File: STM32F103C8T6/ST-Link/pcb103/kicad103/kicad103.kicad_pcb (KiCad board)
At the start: 4 copper layers, 20 parts, among them IC1 LD1117DT33TR, J1 0480372200, J2 Conn_01x02_Socket, U1 STM32F103C8T6, Y1 8MHz 20pF

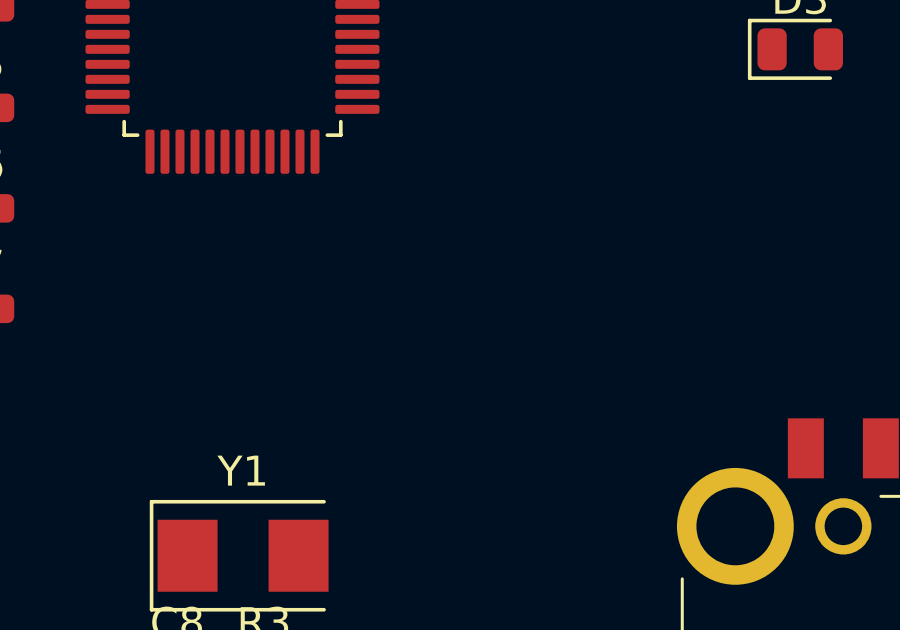
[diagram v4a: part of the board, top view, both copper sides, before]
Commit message: Pull-up resistor on USB_DP line
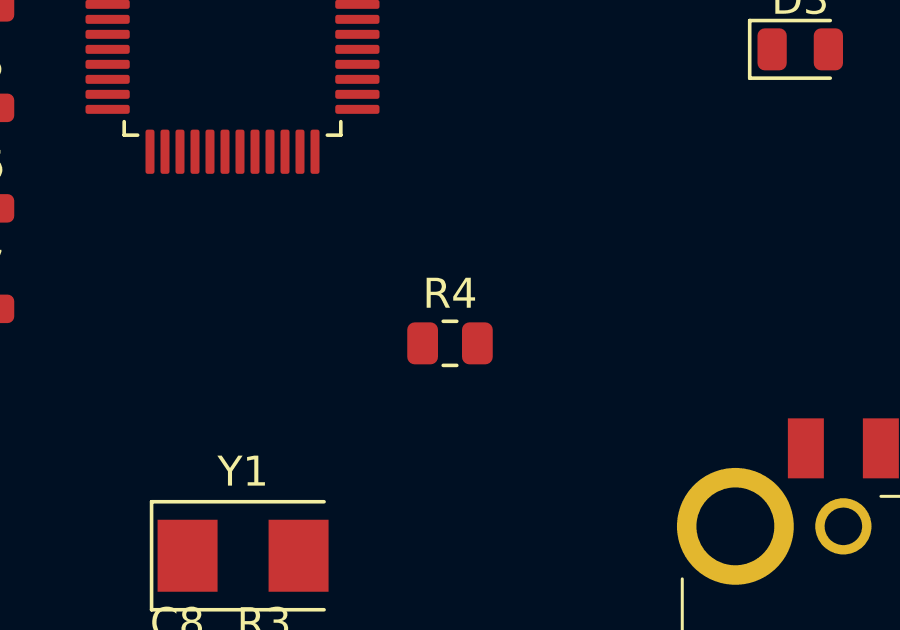
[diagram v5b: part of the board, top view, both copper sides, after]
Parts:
- added R4: 1k5, Resistor_SMD:R_0805_2012Metric, F.Cu at (196.6, 63.7)
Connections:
- net Net-(U1-VBAT) renamed +3.3V
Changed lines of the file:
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@@
   (net 0 "")
   (net 1 "Net-(D1-K)")
-  (net 2 "Net-(U1-VBAT)")
+  (net 2 "+3.3V")
   (net 3 "/USB_D-")
   (net 4 "GND")
@@
       (stroke (width 0.1) (type solid)) (layer "F.Fab"))
     (pad "1" smd roundrect (at -0.775 0) (size 0.9 0.95) (layers "F.Cu" "F.Paste" "F.Mask") (roundrect_rratio 0.25)
-      (net 2 "Net-(U1-VBAT)") (pintype "passive"))
+      (net 2 "+3.3V") (pintype "passive"))
     (pad "2" smd roundrect (at 0.775 0) (size 0.9 0.95) (layers "F.Cu" "F.Paste" "F.Mask") (roundrect_rratio 0.25)
       (net 4 "GND") (pintype "passive"))
@@
       (stroke (width 0.1) (type solid)) (layer "F.Fab"))
     (pad "1" smd roundrect (at -0.775 0) (size 0.9 0.95) (layers "F.Cu" "F.Paste" "F.Mask") (roundrect_rratio 0.25)
-      (net 2 "Net-(U1-VBAT)") (pintype "passive"))
+      (net 2 "+3.3V") (pintype "passive"))
     (pad "2" smd roundrect (at 0.775 0) (size 0.9 0.95) (layers "F.Cu" "F.Paste" "F.Mask") (roundrect_rratio 0.25)
       (net 4 "GND") (pintype "passive"))
@@
       (stroke (width 0.1) (type solid)) (layer "F.Fab"))
     (pad "1" smd roundrect (at -0.775 0) (size 0.9 0.95) (layers "F.Cu" "F.Paste" "F.Mask") (roundrect_rratio 0.25)
-      (net 2 "Net-(U1-VBAT)") (pintype "passive"))
+      (net 2 "+3.3V") (pintype "passive"))
     (pad "2" smd roundrect (at 0.775 0) (size 0.9 0.95) (layers "F.Cu" "F.Paste" "F.Mask") (roundrect_rratio 0.25)
       (net 4 "GND") (pintype "passive"))
@@
       (stroke (width 0.1) (type solid)) (layer "F.Fab"))
     (pad "1" smd roundrect (at -0.775 0) (size 0.9 0.95) (layers "F.Cu" "F.Paste" "F.Mask") (roundrect_rratio 0.25)
-      (net 2 "Net-(U1-VBAT)") (pintype "passive"))
+      (net 2 "+3.3V") (pintype "passive"))
     (pad "2" smd roundrect (at 0.775 0) (size 0.9 0.95) (layers "F.Cu" "F.Paste" "F.Mask") (roundrect_rratio 0.25)
       (net 4 "GND") (pintype "passive"))
@@
       (stroke (width 0.1) (type solid)) (layer "F.Fab"))
     (pad "1" smd roundrect (at -4.1625 -2.75) (size 1.475 0.3) (layers "F.Cu" "F.Paste" "F.Mask") (roundrect_rratio 0.25)
-      (net 2 "Net-(U1-VBAT)") (pinfunction "VBAT") (pintype "power_in"))
+      (net 2 "+3.3V") (pinfunction "VBAT") (pintype "power_in"))
     (pad "2" smd roundrect (at -4.1625 -2.25) (size 1.475 0.3) (layers "F.Cu" "F.Paste" "F.Mask") (roundrect_rratio 0.25)
       (net 50 "Net-(D3-A)") (pinfunction "PC13") (pintype "bidirectional"))
@@
       (net 4 "GND") (pinfunction "VSSA") (pintype "power_in"))
     (pad "9" smd roundrect (at -4.1625 1.25) (size 1.475 0.3) (layers "F.Cu" "F.Paste" "F.Mask") (roundrect_rratio 0.25)
-      (net 2 "Net-(U1-VBAT)") (pinfunction "VDDA") (pintype "power_in"))
+      (net 2 "+3.3V") (pinfunction "VDDA") (pintype "power_in"))
     (pad "10" smd roundrect (at -4.1625 1.75) (size 1.475 0.3) (layers "F.Cu" "F.Paste" "F.Mask") (roundrect_rratio 0.25)
       (net 18 "unconnected-(U1-PA0-Pad10)") (pinfunction "PA0") (pintype "bidirectional+no_connect"))
@@
       (net 4 "GND") (pinfunction "VSS") (pintype "power_in"))
     (pad "24" smd roundrect (at 2.75 4.1625) (size 0.3 1.475) (layers "F.Cu" "F.Paste" "F.Mask") (roundrect_rratio 0.25)
-      (net 2 "Net-(U1-VBAT)") (pinfunction "VDD") (pintype "power_in"))
+      (net 2 "+3.3V") (pinfunction "VDD") (pintype "power_in"))
     (pad "25" smd roundrect (at 4.1625 2.75) (size 1.475 0.3) (layers "F.Cu" "F.Paste" "F.Mask") (roundrect_rratio 0.25)
       (net 31 "unconnected-(U1-PB12-Pad25)") (pinfunction "PB12") (pintype "bidirectional+no_connect"))
@@
       (net 4 "GND") (pinfunction "VSS") (pintype "passive"))
     (pad "36" smd roundrect (at 4.1625 -2.75) (size 1.475 0.3) (layers "F.Cu" "F.Paste" "F.Mask") (roundrect_rratio 0.25)
-      (net 2 "Net-(U1-VBAT)") (pinfunction "VDD") (pintype "power_in"))
+      (net 2 "+3.3V") (pinfunction "VDD") (pintype "power_in"))
     (pad "37" smd roundrect (at 2.75 -4.1625) (size 0.3 1.475) (layers "F.Cu" "F.Paste" "F.Mask") (roundrect_rratio 0.25)
       (net 39 "unconnected-(U1-PA14-Pad37)") (pinfunction "PA14") (pintype "bidirectional+no_connect"))
@@
       (net 4 "GND") (pinfunction "VSS") (pintype "passive"))
     (pad "48" smd roundrect (at -2.75 -4.1625) (size 0.3 1.475) (layers "F.Cu" "F.Paste" "F.Mask") (roundrect_rratio 0.25)
-      (net 2 "Net-(U1-VBAT)") (pinfunction "VDD") (pintype "power_in"))
+      (net 2 "+3.3V") (pinfunction "VDD") (pintype "power_in"))
     (model "${KICAD6_3DMODEL_DIR}/Package_QFP.3dshapes/LQFP-48_7x7mm_P0.5mm.wrl"
       (offset (xyz 0 0 0))
@@
     )
   )
+  (footprint "Resistor_SMD:R_0805_2012Metric" (layer "F.Cu")
+    (at 196.5875 63.7)
+    (descr "Resistor SMD 0805 (2012 Metric), square (rectangular) end terminal, IPC_7351 nominal, (Body size source: IPC-SM-782 page 72, https://www.pcb-3d.com/wordpress/wp-content/uploads/ipc-sm-782a_amendment_1_and_2.pdf), generated with kicad-footprint-generator")
+    (tags "resistor")
+    (property "Sheetfile" "kicad103.kicad_sch")
+    (property "Sheetname" "")
+    (property "ki_description" "Resistor")
+    (property "ki_keywords" "R res resistor")
+    (attr smd)
+    (fp_text reference "R4" (at 0 -1.65) (layer "F.SilkS")
+        (effects (font (size 1 1) (thickness 0.15)))
+    )
+    (fp_text value "1k5" (at 0 1.65) (layer "F.Fab")
+        (effects (font (size 1 1) (thickness 0.15)))
+    )
+    (fp_text user "${REFERENCE}" (at 0 0) (layer "F.Fab")
+        (effects (font (size 0.5 0.5) (thickness 0.08)))
+    )
+    (fp_line (start -0.227064 -0.735) (end 0.227064 -0.735)
+      (stroke (width 0.12) (type solid)) (layer "F.SilkS"))
+    (fp_line (start -0.227064 0.735) (end 0.227064 0.735)
+      (stroke (width 0.12) (type solid)) (layer "F.SilkS"))
+    (fp_line (start -1.68 -0.95) (end 1.68 -0.95)
+      (stroke (width 0.05) (type solid)) (layer "F.CrtYd"))
+    (fp_line (start -1.68 0.95) (end -1.68 -0.95)
+      (stroke (width 0.05) (type solid)) (layer "F.CrtYd"))
+    (fp_line (start 1.68 -0.95) (end 1.68 0.95)
+      (stroke (width 0.05) (type solid)) (layer "F.CrtYd"))
+    (fp_line (start 1.68 0.95) (end -1.68 0.95)
+      (stroke (width 0.05) (type solid)) (layer "F.CrtYd"))
+    (fp_line (start -1 -0.625) (end 1 -0.625)
+      (stroke (width 0.1) (type solid)) (layer "F.Fab"))
+    (fp_line (start -1 0.625) (end -1 -0.625)
+      (stroke (width 0.1) (type solid)) (layer "F.Fab"))
+    (fp_line (start 1 -0.625) (end 1 0.625)
+      (stroke (width 0.1) (type solid)) (layer "F.Fab"))
+    (fp_line (start 1 0.625) (end -1 0.625)
+      (stroke (width 0.1) (type solid)) (layer "F.Fab"))
+    (pad "1" smd roundrect (at -0.9125 0) (size 1.025 1.4) (layers "F.Cu" "F.Paste" "F.Mask") (roundrect_rratio 0.243902)
+      (net 2 "+3.3V") (pintype "passive"))
+    (pad "2" smd roundrect (at 0.9125 0) (size 1.025 1.4) (layers "F.Cu" "F.Paste" "F.Mask") (roundrect_rratio 0.243902)
+      (net 11 "/USB_D+") (pintype "passive"))
+    (model "${KICAD6_3DMODEL_DIR}/Resistor_SMD.3dshapes/R_0805_2012Metric.wrl"
+      (offset (xyz 0 0 0))
+      (scale (xyz 1 1 1))
+      (rotate (xyz 0 0 0))
+    )
+  )
   (footprint "LED_SMD:LED_0805_2012Metric" (layer "F.Cu")
     (at 225.2625 66.4)
@@
       (stroke (width 0.1) (type solid)) (layer "F.Fab"))
     (pad "1" smd roundrect (at -0.775 0) (size 0.9 0.95) (layers "F.Cu" "F.Paste" "F.Mask") (roundrect_rratio 0.25)
-      (net 2 "Net-(U1-VBAT)") (pintype "passive"))
+      (net 2 "+3.3V") (pintype "passive"))
     (pad "2" smd roundrect (at 0.775 0) (size 0.9 0.95) (layers "F.Cu" "F.Paste" "F.Mask") (roundrect_rratio 0.25)
       (net 4 "GND") (pintype "passive"))

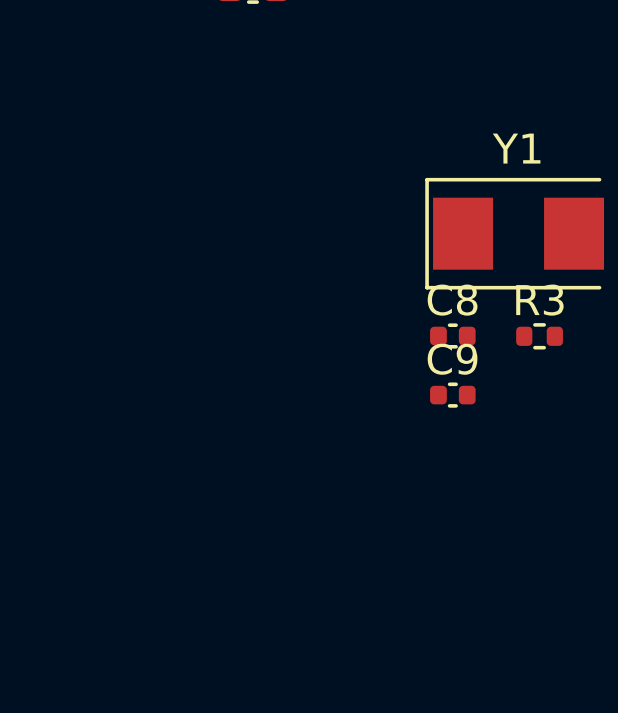
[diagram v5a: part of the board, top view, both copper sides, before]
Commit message: Add JTAG
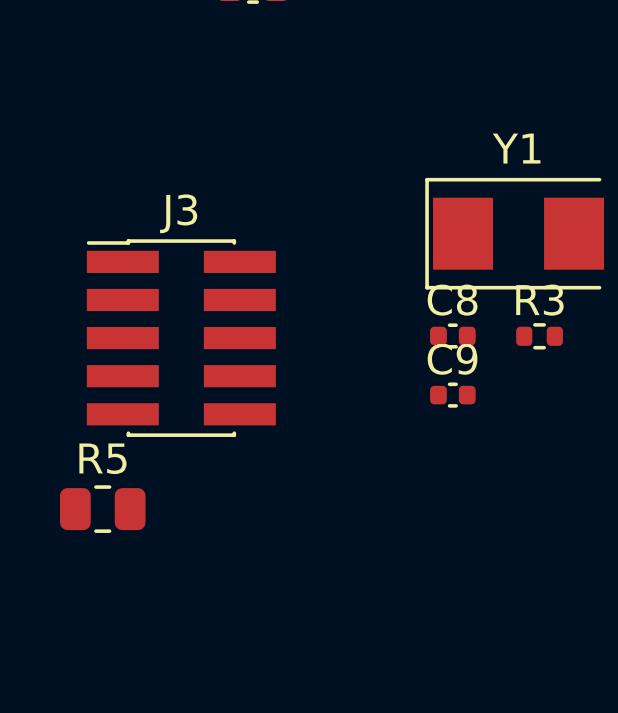
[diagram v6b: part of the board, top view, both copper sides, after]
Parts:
- added J3: Conn_02x05_Odd_Even, Connector_PinHeader_1.27mm:PinHeader_2x05_P1.27mm_Vertical_SMD, F.Cu at (178.4, 74.3)
- added R5: 1k5, Resistor_SMD:R_0805_2012Metric, F.Cu at (175.8, 80.0)
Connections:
- U1 pad 34: unconnected-(U1-PA13-Pad34) -> Net-(J3-Pin_2)
- U1 pad 37: unconnected-(U1-PA14-Pad37) -> Net-(J3-Pin_4)
- U1 pad 38: unconnected-(U1-PA15-Pad38) -> Net-(J3-Pin_8)
- U1 pad 39: unconnected-(U1-PB3-Pad39) -> Net-(J3-Pin_6)
- U1 pad 44: unconnected-(U1-BOOT0-Pad44) -> Net-(U1-BOOT0)
- U1 pad 7: unconnected-(U1-NRST-Pad7) -> Net-(J3-Pin_10)

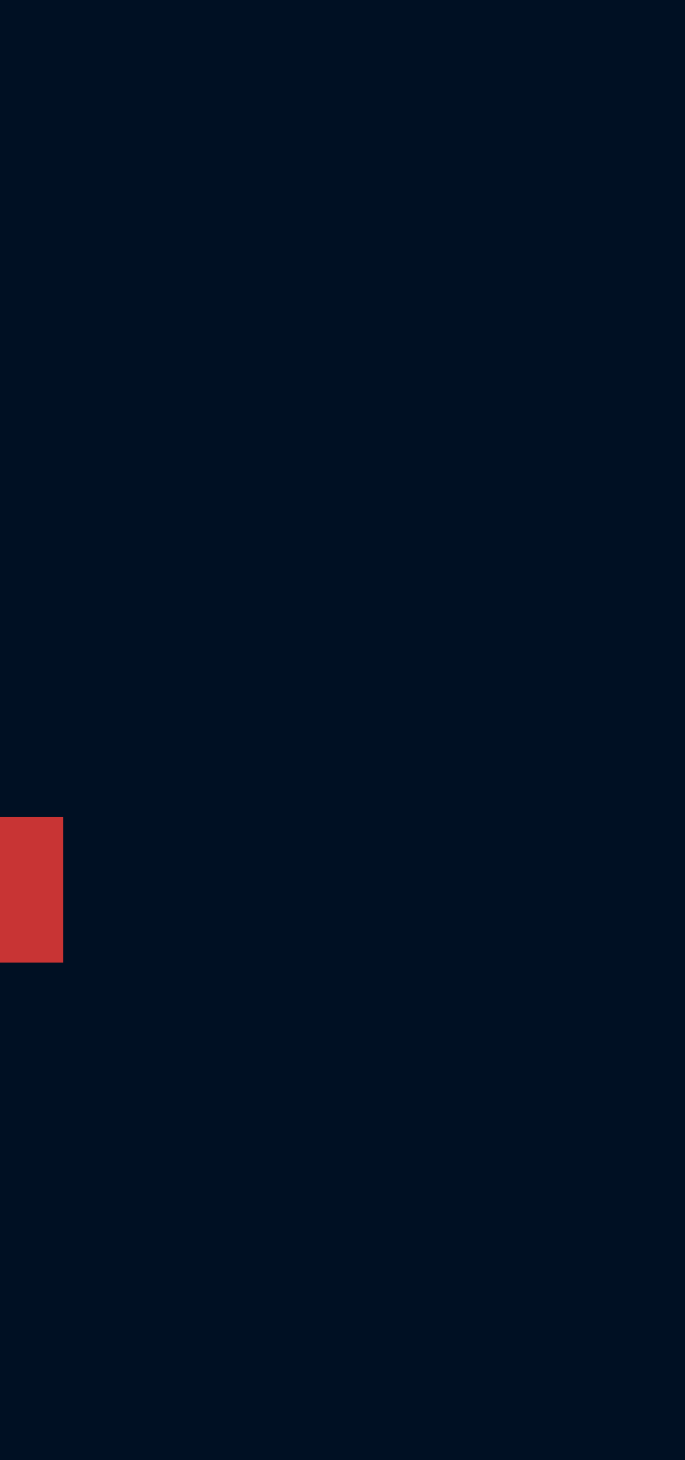
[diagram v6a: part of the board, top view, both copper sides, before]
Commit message: Remaining pins
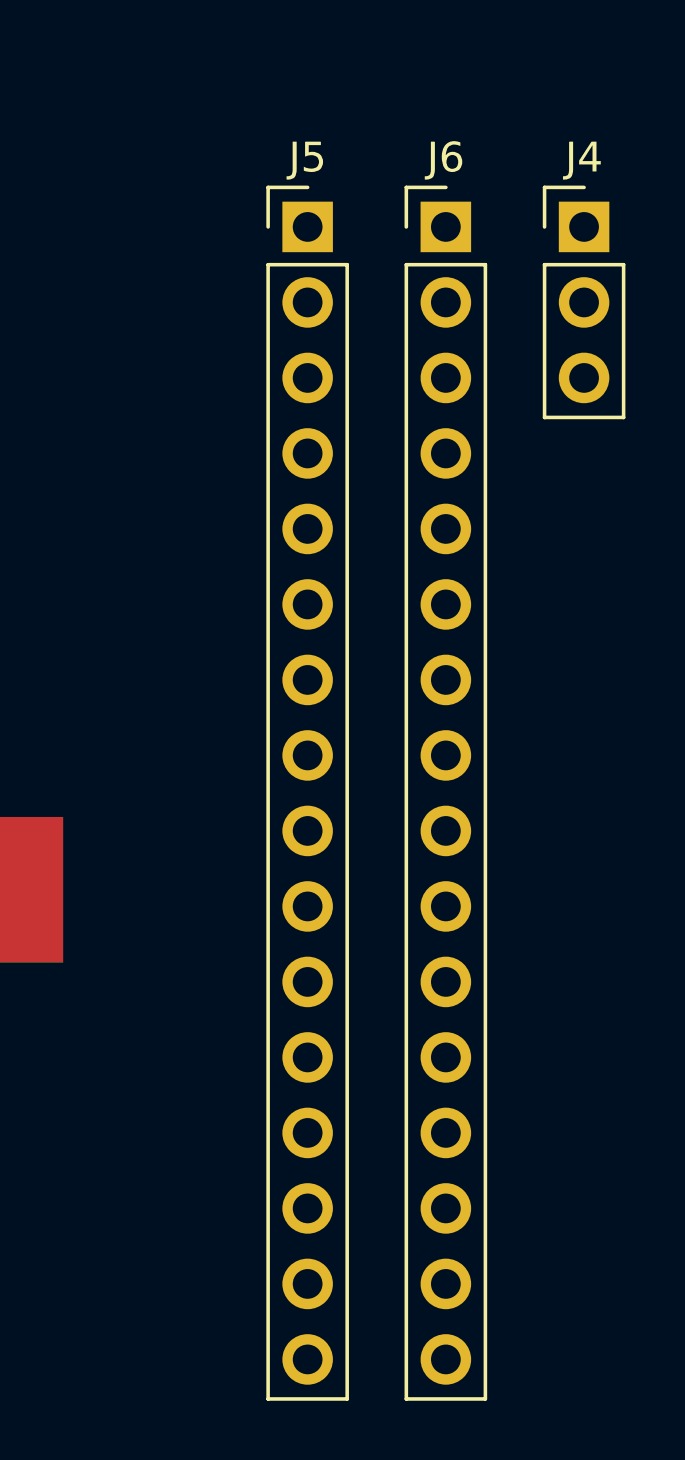
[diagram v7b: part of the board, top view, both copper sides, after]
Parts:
- added J4: Conn_01x03_Pin, Connector_PinHeader_2.54mm:PinHeader_1x03_P2.54mm_Vertical, F.Cu at (259.2, 51.9)
- added J5: Conn_01x16_Pin, Connector_PinHeader_2.54mm:PinHeader_1x16_P2.54mm_Vertical, F.Cu at (249.9, 51.9)
- added J6: Conn_01x16_Pin, Connector_PinHeader_2.54mm:PinHeader_1x16_P2.54mm_Vertical, F.Cu at (254.6, 51.9)
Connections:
- net Net-(D3-A) renamed PC13
- net Net-(J3-Pin_2) renamed PA13
- net Net-(J3-Pin_4) renamed PA14
- net Net-(J3-Pin_6) renamed PB3
- net Net-(J3-Pin_8) renamed PA15
- U1 pad 10: unconnected-(U1-PA0-Pad10) -> PA0
- U1 pad 11: unconnected-(U1-PA1-Pad11) -> PA1
- U1 pad 12: unconnected-(U1-PA2-Pad12) -> PA2
- U1 pad 13: unconnected-(U1-PA3-Pad13) -> PA3
- U1 pad 14: unconnected-(U1-PA4-Pad14) -> PA4
- U1 pad 15: unconnected-(U1-PA5-Pad15) -> PA5
- U1 pad 16: unconnected-(U1-PA6-Pad16) -> PA6
- U1 pad 17: unconnected-(U1-PA7-Pad17) -> PA7
- U1 pad 18: unconnected-(U1-PB0-Pad18) -> PB0
- U1 pad 19: unconnected-(U1-PB1-Pad19) -> PB1
- U1 pad 20: unconnected-(U1-PB2-Pad20) -> PB2
- U1 pad 21: unconnected-(U1-PB10-Pad21) -> PB10
- U1 pad 22: unconnected-(U1-PB11-Pad22) -> PB11
- U1 pad 25: unconnected-(U1-PB12-Pad25) -> PB12
- U1 pad 26: unconnected-(U1-PB13-Pad26) -> PB13
- U1 pad 27: unconnected-(U1-PB14-Pad27) -> PB14
- U1 pad 28: unconnected-(U1-PB15-Pad28) -> PB15
- U1 pad 29: unconnected-(U1-PA8-Pad29) -> PA8
- U1 pad 3: unconnected-(U1-PC14-Pad3) -> PC14
- U1 pad 30: unconnected-(U1-PA9-Pad30) -> PA9
- U1 pad 31: unconnected-(U1-PA10-Pad31) -> PA10
- U1 pad 4: unconnected-(U1-PC15-Pad4) -> PC15
- U1 pad 40: unconnected-(U1-PB4-Pad40) -> PB4
- U1 pad 41: unconnected-(U1-PB5-Pad41) -> PB5
- U1 pad 42: unconnected-(U1-PB6-Pad42) -> PB6
- U1 pad 43: unconnected-(U1-PB7-Pad43) -> PB7
- U1 pad 45: unconnected-(U1-PB8-Pad45) -> PB8
- U1 pad 46: unconnected-(U1-PB9-Pad46) -> PB9

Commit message: SWO/SWD
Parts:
- added J7: Conn_01x04_Pin, Connector_PinHeader_2.54mm:PinHeader_1x04_P2.54mm_Vertical, F.Cu at (194.7, 87.3)
- added J8: Conn_01x05_Socket, Connector_PinSocket_2.54mm:PinSocket_1x05_P2.54mm_Vertical, F.Cu at (190.1, 87.3)
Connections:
- D2 pad 1: Net-(D2-K) -> +3.3V
- R1 pad 1: Net-(D2-K) -> +3.3V
